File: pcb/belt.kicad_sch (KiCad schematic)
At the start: 2 parts, among them U1 Raspberry-Pi-Pico, U2 Barometer-KP212K1409XTMA1

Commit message: added thermometer
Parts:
- added U3: Thermometer-LM335D, BeltFootprints:Thermometer-LM335D, symbol Thermometer-LM335D:Thermometer-LM335D
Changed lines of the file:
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@@
   (title_block
     (title "Basic Electronics Learning Toolkit")
-    (date "2023-12-25")
+    (date "2023-12-26")
     (rev "0.1")
     (company "Rice Eclipse")
@@
         )
       )
+    )
+  )
+  (symbol (lib_id "Thermometer-LM335D:Thermometer-LM335D") (at 177.8 93.98 0) (unit 1)
+    (in_bom yes) (on_board yes) (dnp no) (fields_autoplaced)
+    (property "Reference" "U3" (at 177.8 73.66 0)
+      (effects (font (size 1.27 1.27)))
+    )
+    (property "Value" "Thermometer-LM335D" (at 177.8 76.2 0)
+      (effects (font (size 1.27 1.27)))
+    )
+    (property "Footprint" "BeltFootprints:Thermometer-LM335D" (at 177.8 116.84 0) (show_name)
+      (effects (font (size 1.27 1.27)) hide)
+    )
+    (property "Datasheet" "https://www.st.com/content/ccc/resource/technical/document/datasheet/04/fa/9d/16/39/87/44/8d/CD00000459.pdf/files/CD00000459.pdf/jcr:content/translations/en.CD00000459.pdf" (at 177.8 119.38 0) (show_name)
+      (effects (font (size 1.27 1.27)) hide)
+    )
+    (property "Manufacturer" "STMicroelectronics" (at 177.8 121.92 0) (show_name)
+      (effects (font (size 1.27 1.27)) hide)
+    )
+    (property "Part Number" "LM335D" (at 177.8 124.46 0) (show_name)
+      (effects (font (size 1.27 1.27)) hide)
+    )
+    (pin "1")
+    (pin "2")
+    (pin "3")
+    (pin "4")
+    (pin "5")
+    (pin "6")
+    (pin "7")
+    (pin "8")
+    (instances
+      (project "belt"
+        (path "/33e5c18d-f516-4ab7-aaea-c68685305111"
+          (reference "U3") (unit 1)
+        )
+      )

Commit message: wired things up
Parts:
- added R1: 3.9k, symbol Device:R
- added SW1: RESET, symbol Switch:SW_Push_Dual
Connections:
- net +5V: now reaches U2.5 (VDD)
- net +5V: now also U1.39 (VSYS), R1.1
- net GND: now reaches U2.6 (GND_1)
- net GND: now also U1.13 (GND), U1.18 (GND), U1.23 (GND), U1.28 (GND), U1.3 (GND), U1.38 (GND), U1.8 (GND), U1.D2 (GND), U2.8 (GND_2), U3.4 (V-), SW1.2, SW1.4
- net BaroData: now reaches U2.7 (VOUT)
- net BaroData: now also U1.31 (GP26)
- net PicoNReset: now reaches U1.30 (~{RUN})
- net PicoNReset: now also SW1.1, SW1.3
- net TempData: now reaches U1.32 (GP27)
- net TempData: now also U3.8 (V+), R1.2
- net GNDA: now reaches U1.33 (AGND)
- net GNDA: now also U1.34 (GP28)
- net +3.3V: now reaches U1.35 (ADC_VREF)
- net +3.3V: now also U1.36 (3V3_OUT)
- net VBUS: now reaches U1.40 (VBUS)
- no-connect marks 0 -> 37
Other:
- note added: "TODO: - Add decoupling caps - BaroData signal processing - TempData voltage divider - Add prot diodes - Add any needed pullups/downs - Add lipo connector?? - Thermometer calibration pot? - Barometer calibration?? - Add indicator LEDs"
- moved on the sheet: U1, U2, U3

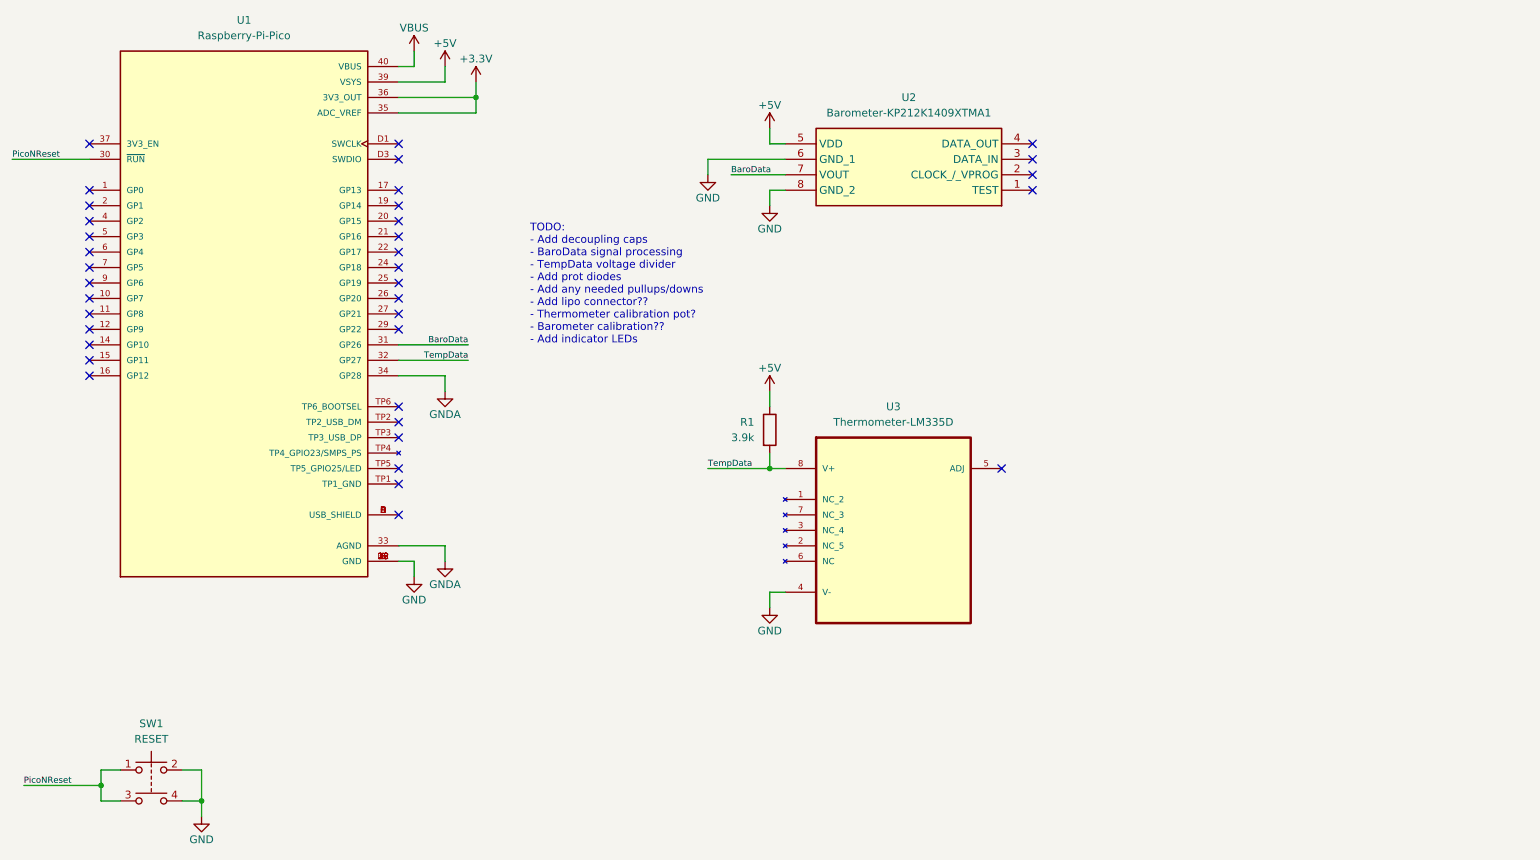
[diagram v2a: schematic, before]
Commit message: added voltdivs and schematic pages
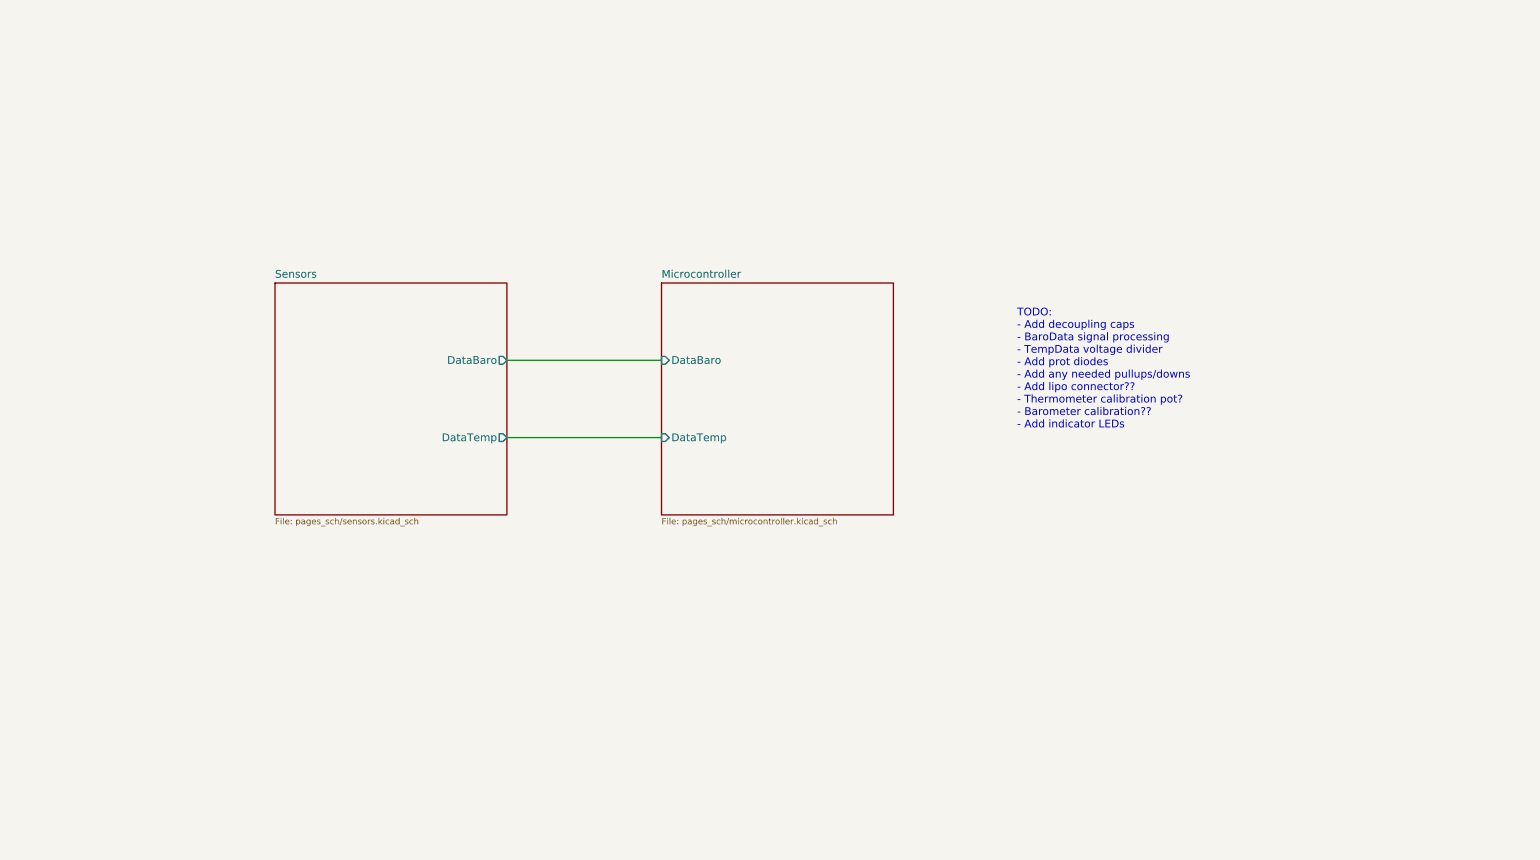
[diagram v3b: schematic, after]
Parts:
- removed R1: 3.9k, symbol Device:R
- removed SW1: RESET, symbol Switch:SW_Push_Dual
- removed U1: Raspberry-Pi-Pico, BeltFootprints:Raspberry-Pi-Pico, symbol Raspberry-Pi-Pico:Raspberry-Pi-Pico
- removed U2: Barometer-KP212K1409XTMA1, BeltFootprints:Barometer-KP212K1409XTMA1, symbol Barometer-KP212K1409XTMA1:Barometer-KP212K1409XTMA1
- removed U3: Thermometer-LM335D, BeltFootprints:Thermometer-LM335D, symbol Thermometer-LM335D:Thermometer-LM335D
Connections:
- no-connect marks 37 -> 0
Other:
- added sheet Microcontroller (pages_sch/microcontroller.kicad_sch)
- added sheet Sensors (pages_sch/sensors.kicad_sch)

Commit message: renamed dirs
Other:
- sheet Microcontroller: file pages_sch/microcontroller.kicad_sch -> subsheets/microcontroller.kicad_sch
- sheet Sensors: file pages_sch/sensors.kicad_sch -> subsheets/sensors.kicad_sch
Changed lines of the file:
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@@
       (effects (font (size 1.27 1.27)) (justify left bottom))
     )
-    (property "Sheetfile" "pages_sch/microcontroller.kicad_sch" (at 127 102.083 0)
+    (property "Sheetfile" "subsheets/microcontroller.kicad_sch" (at 127 102.083 0)
       (effects (font (size 1.016 1.016)) (justify left top))
     )
@@
       (effects (font (size 1.27 1.27)) (justify left bottom))
     )
-    (property "Sheetfile" "pages_sch/sensors.kicad_sch" (at 63.5 102.083 0)
+    (property "Sheetfile" "subsheets/sensors.kicad_sch" (at 63.5 102.083 0)
       (effects (font (size 1.016 1.016)) (justify left top))
     )

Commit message: fixed everything (ERC is no longer mad)
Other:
- sheet Microcontroller ports: added SCL_{0}, SDA_{0}, V_{ADC0}; removed DataBaro, DataTemp
- sheet Sensors ports: added Thermo_SCL, Thermo_SDA, V_{baro}; removed DataBaro, DataTemp
- note added: "TODO: - Add decoupling caps - Add prot diodes - Add any needed pullups/downs - Add lipo connector?? - Barometer calibration?? - Add baro LPF?? - Add indicator LEDs - Add mounting holes"
- note removed: "TODO: - Add decoupling caps - BaroData signal processing - TempData voltage divider - Add prot diodes - Add any needed pullups/downs - Add lipo connector?? - Thermometer calibration pot? - Barometer calibration?? - Add indicator LEDs"
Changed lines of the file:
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@@
   (title_block
     (title "Basic Electronics Learning Toolkit")
-    (date "2023-12-27")
-    (rev "0.1")
+    (date "2023-12-31")
+    (rev "0.2")
     (company "Rice Eclipse")
+    (comment 1 "Adam Sher")
   )
-  (wire (pts (xy 101.6 88.9) (xy 127 88.9))
+  (wire (pts (xy 101.6 91.44) (xy 127 91.44))
+    (stroke (width 0) (type default))
+  )
+  (wire (pts (xy 101.6 86.36) (xy 127 86.36))
     (stroke (width 0) (type default))
   )
@@
     (stroke (width 0) (type default))
   )
-  (text "TODO: \n- Add decoupling caps\n- BaroData signal processing\n- TempData voltage divider\n- Add prot diodes\n- Add any needed pullups/downs\n- Add lipo connector??\n- Thermometer calibration pot?\n- Barometer calibration??\n- Add indicator LEDs"
+  (text "TODO: \n- Add decoupling caps\n- Add prot diodes\n- Add any needed pullups/downs\n- Add lipo connector??\n- Barometer calibration??\n- Add baro LPF??\n- Add indicator LEDs\n- Add mounting holes"
     (at 185.42 87.63 0)
     (effects (font (size 1.27 1.27)) (justify left bottom))
   )
-  (sheet (at 127 63.5) (size 38.1 38.1) (fields_autoplaced)
+  (sheet (at 127 63.5) (size 38.1 38.1)
     (stroke (width 0.1524) (type solid))
     (fill (color 0 0 0 0.0000))
-    (property "Sheetname" "Microcontroller" (at 127 62.7884 0)
-      (effects (font (size 1.27 1.27)) (justify left bottom))
+    (property "Sheetname" "Microcontroller" (at 146.05 66.04 0) (do_not_autoplace)
+      (effects (font (size 3.175 3.175) bold) (justify top))
     )
     (property "Sheetfile" "subsheets/microcontroller.kicad_sch" (at 127 102.083 0)
       (effects (font (size 1.016 1.016)) (justify left top))
     )
-    (pin "DataTemp" input (at 127 88.9 180)
+    (pin "V_{ADC0}" input (at 127 76.2 180)
       (effects (font (size 1.27 1.27)) (justify left))
     )
-    (pin "DataBaro" input (at 127 76.2 180)
+    (pin "SDA_{0}" bidirectional (at 127 86.36 180)
+      (effects (font (size 1.27 1.27)) (justify left))
+    )
+    (pin "SCL_{0}" output (at 127 91.44 180)
       (effects (font (size 1.27 1.27)) (justify left))
     )
@@
     )
   )
-  (sheet (at 63.5 63.5) (size 38.1 38.1) (fields_autoplaced)
+  (sheet (at 63.5 63.5) (size 38.1 38.1)
     (stroke (width 0.1524) (type solid))
     (fill (color 0 0 0 0.0000))
-    (property "Sheetname" "Sensors" (at 63.5 62.7884 0)
-      (effects (font (size 1.27 1.27)) (justify left bottom))
+    (property "Sheetname" "Sensors" (at 82.55 66.04 0) (do_not_autoplace)
+      (effects (font (size 3.175 3.175) bold) (justify top))
     )
     (property "Sheetfile" "subsheets/sensors.kicad_sch" (at 63.5 102.083 0)
       (effects (font (size 1.016 1.016)) (justify left top))
     )
-    (pin "DataBaro" output (at 101.6 76.2 0)
+    (pin "V_{baro}" output (at 101.6 76.2 0)
       (effects (font (size 1.27 1.27)) (justify right))
     )
-    (pin "DataTemp" output (at 101.6 88.9 0)
+    (pin "Thermo_SDA" bidirectional (at 101.6 86.36 0)
       (effects (font (size 1.27 1.27)) (justify right))
     )
+    (pin "Thermo_SCL" input (at 101.6 91.44 0)
+      (effects (font (size 1.27 1.27)) (justify right))
+    )

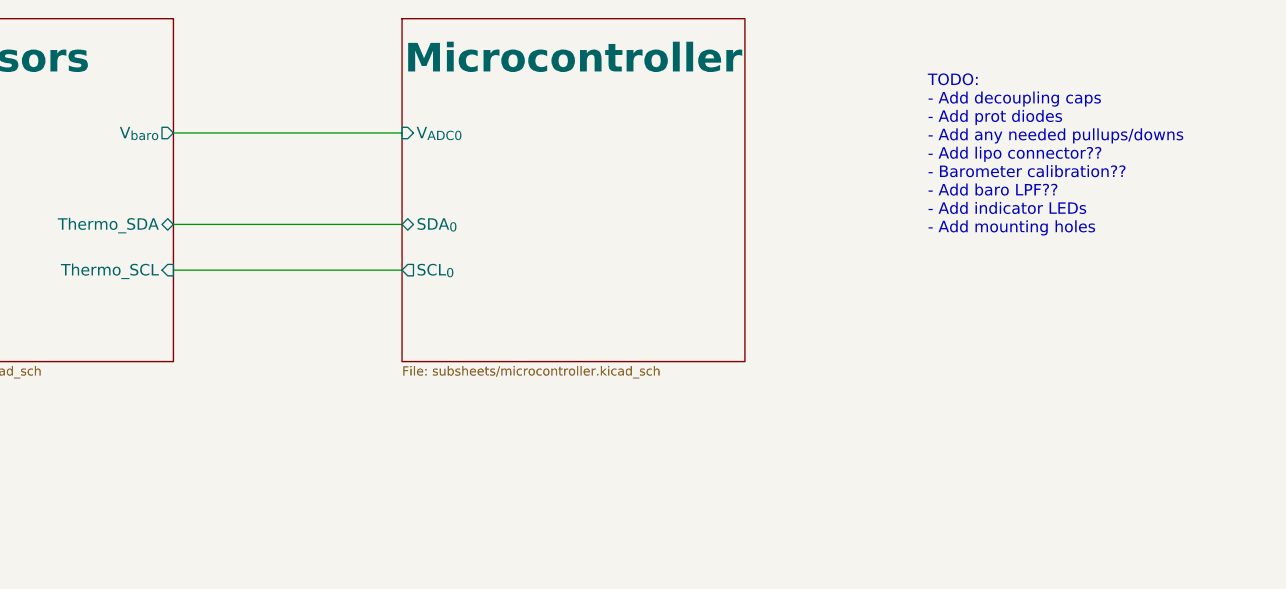
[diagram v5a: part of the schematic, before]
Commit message: fixed all the resistors
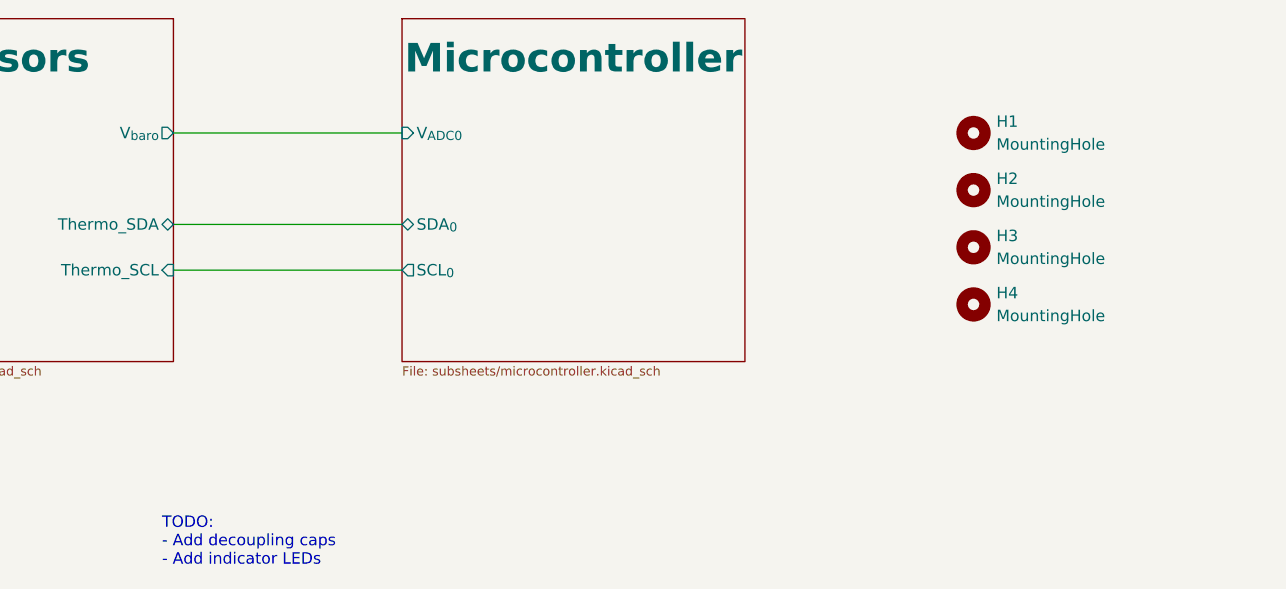
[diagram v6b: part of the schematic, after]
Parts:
- added H1, H2, H3, H4: MountingHole, symbol Mechanical:MountingHole
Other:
- note added: "TODO: - Add decoupling caps - Add indicator LEDs"
- note removed: "TODO: - Add decoupling caps - Add prot diodes - Add any needed pullups/downs - Add lipo connector?? - Barometer calibration?? - Add baro LPF?? - Add indicator LEDs - Add mounting holes"
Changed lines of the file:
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@@
     (stroke (width 0) (type default))
   )
-  (text "TODO: \n- Add decoupling caps\n- Add prot diodes\n- Add any needed pullups/downs\n- Add lipo connector??\n- Barometer calibration??\n- Add baro LPF??\n- Add indicator LEDs\n- Add mounting holes"
-    (at 185.42 87.63 0)
+  (text "TODO: \n- Add decoupling caps\n- Add indicator LEDs" (at 100.33 124.46 0)
     (effects (font (size 1.27 1.27)) (justify left bottom))
   )
+  (symbol (lib_id "Mechanical:MountingHole") (at 190.5 76.2 0) (unit 1)
+    (in_bom yes) (on_board yes) (dnp no) (fields_autoplaced)
+    (property "Reference" "H1" (at 193.04 74.93 0)
+      (effects (font (size 1.27 1.27)) (justify left))
+    )
+    (property "Value" "MountingHole" (at 193.04 77.47 0)
+      (effects (font (size 1.27 1.27)) (justify left))
+    )
+    (property "Footprint" "" (at 190.5 76.2 0)
+      (effects (font (size 1.27 1.27)) hide)
+    )
+    (property "Datasheet" "~" (at 190.5 76.2 0)
+      (effects (font (size 1.27 1.27)) hide)
+    )
+    (instances
+      (project "belt"
+        (path "/33e5c18d-f516-4ab7-aaea-c68685305111"
+          (reference "H1") (unit 1)
+        )
+      )
+    )
+  )
+  (symbol (lib_id "Mechanical:MountingHole") (at 190.5 88.9 0) (unit 1)
+    (in_bom yes) (on_board yes) (dnp no) (fields_autoplaced)
+    (property "Reference" "H3" (at 193.04 87.63 0)
+      (effects (font (size 1.27 1.27)) (justify left))
+    )
+    (property "Value" "MountingHole" (at 193.04 90.17 0)
+      (effects (font (size 1.27 1.27)) (justify left))
+    )
+    (property "Footprint" "" (at 190.5 88.9 0)
+      (effects (font (size 1.27 1.27)) hide)
+    )
+    (property "Datasheet" "~" (at 190.5 88.9 0)
+      (effects (font (size 1.27 1.27)) hide)
+    )
+    (instances
+      (project "belt"
+        (path "/33e5c18d-f516-4ab7-aaea-c68685305111"
+          (reference "H3") (unit 1)
+        )
+      )
+    )
+  )
+  (symbol (lib_id "Mechanical:MountingHole") (at 190.5 95.25 0) (unit 1)
+    (in_bom yes) (on_board yes) (dnp no) (fields_autoplaced)
+    (property "Reference" "H4" (at 193.04 93.98 0)
+      (effects (font (size 1.27 1.27)) (justify left))
+    )
+    (property "Value" "MountingHole" (at 193.04 96.52 0)
+      (effects (font (size 1.27 1.27)) (justify left))
+    )
+    (property "Footprint" "" (at 190.5 95.25 0)
+      (effects (font (size 1.27 1.27)) hide)
+    )
+    (property "Datasheet" "~" (at 190.5 95.25 0)
+      (effects (font (size 1.27 1.27)) hide)
+    )
+    (instances
+      (project "belt"
+        (path "/33e5c18d-f516-4ab7-aaea-c68685305111"
+          (reference "H4") (unit 1)
+        )
+      )
+    )
+  )
+  (symbol (lib_id "Mechanical:MountingHole") (at 190.5 82.55 0) (unit 1)
+    (in_bom yes) (on_board yes) (dnp no) (fields_autoplaced)
+    (property "Reference" "H2" (at 193.04 81.28 0)
+      (effects (font (size 1.27 1.27)) (justify left))
+    )
+    (property "Value" "MountingHole" (at 193.04 83.82 0)
+      (effects (font (size 1.27 1.27)) (justify left))
+    )
+    (property "Footprint" "" (at 190.5 82.55 0)
+      (effects (font (size 1.27 1.27)) hide)
+    )
+    (property "Datasheet" "~" (at 190.5 82.55 0)
+      (effects (font (size 1.27 1.27)) hide)
+    )
+    (instances
+      (project "belt"
+        (path "/33e5c18d-f516-4ab7-aaea-c68685305111"
+          (reference "H2") (unit 1)
+        )
+      )
+    )
+  )
   (sheet (at 127 63.5) (size 38.1 38.1)
